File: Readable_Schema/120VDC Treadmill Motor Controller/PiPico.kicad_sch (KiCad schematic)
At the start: 6 parts, among them J3 TB0011-350-08BE, J4 TB0011-350-08BE, J5 TB0011-350-08BE

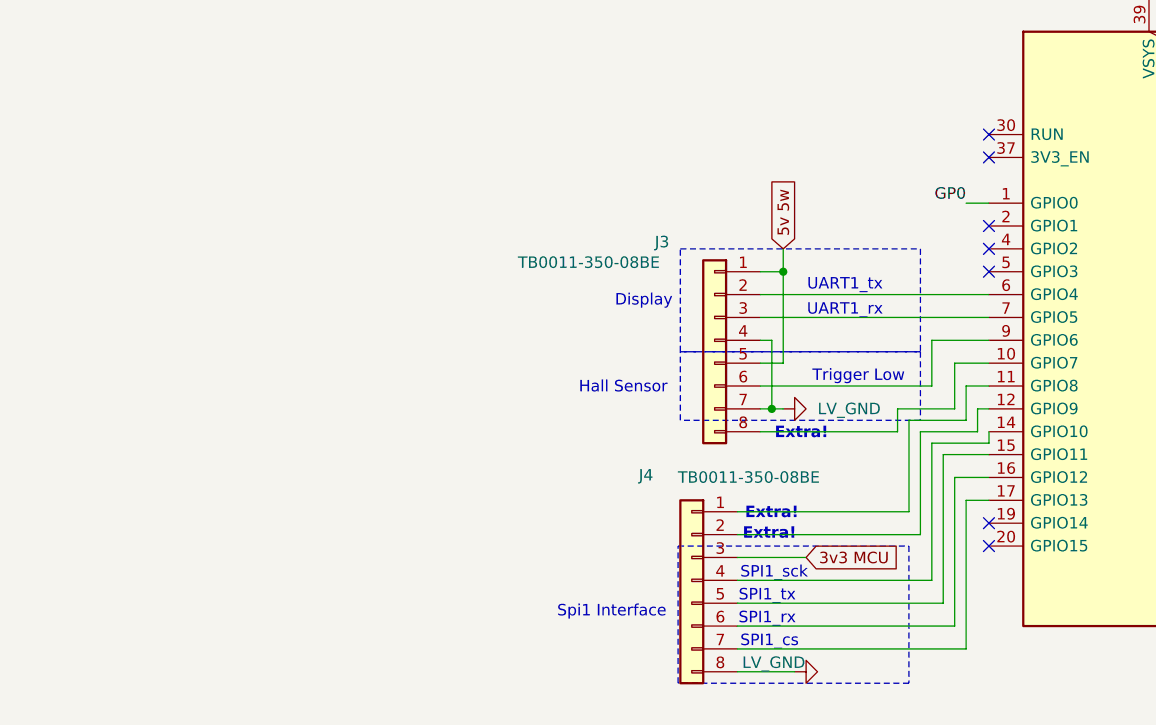
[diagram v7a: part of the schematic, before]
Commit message: -Feedback Schema --fixed some of fine details surrounding pulling some stuff to ground --missing bypass caps --resizing footprints
-H bridge
--Chose higher current rating schottky diode
--Resized footprints and chose better
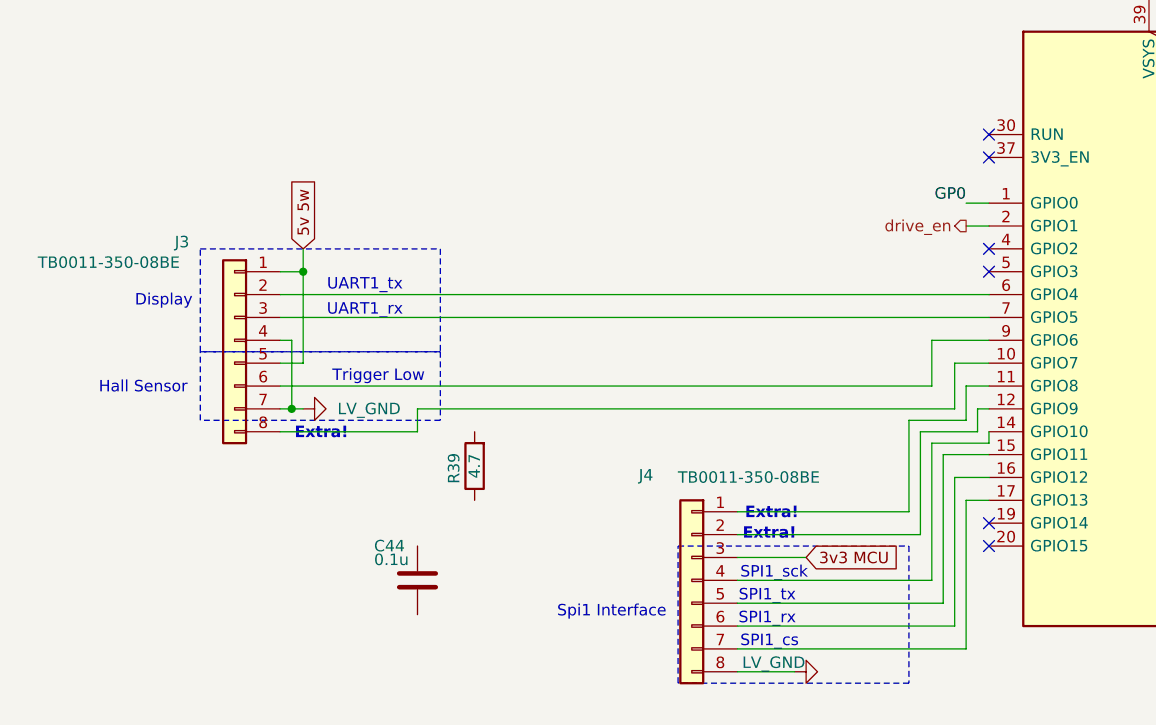
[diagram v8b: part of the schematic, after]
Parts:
- added C44: 0.1u, Capacitor_SMD:C_0201_0603Metric_Pad0.64x0.40mm_HandSolder, symbol Device:C
- added R39: 4.7, Resistor_SMD:R_0201_0603Metric_Pad0.64x0.40mm_HandSolder, symbol Device:R
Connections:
- net drive_en: now reaches A1.2 (GPIO1)
- no-connect marks 9 -> 8
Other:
- moved on the sheet: J3
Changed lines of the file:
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@@
 	(paper "A4")
 	(rectangle
-		(start 83.82 90.17)
-		(end 110.49 101.6)
+		(start 30.48 90.17)
+		(end 57.15 101.6)
 		(stroke
 			(width 0)
@@
 	)
 	(rectangle
-		(start 83.82 101.6)
-		(end 110.49 109.22)
+		(start 30.48 101.6)
+		(end 57.15 109.22)
 		(stroke
 			(width 0)
@@
 	(text "Hall Sensor"
 		(exclude_from_sim no)
-		(at 77.47 105.664 0)
+		(at 24.13 105.664 0)
 		(effects
 			(font
@@
 	(text "UART1_tx"
 		(exclude_from_sim no)
-		(at 102.108 94.234 0)
+		(at 48.768 94.234 0)
 		(effects
 			(font
@@
 	(text "UART1_rx"
 		(exclude_from_sim no)
-		(at 102.108 97.028 0)
+		(at 48.768 97.028 0)
 		(effects
 			(font
@@
 	(text "Display"
 		(exclude_from_sim no)
-		(at 79.756 96.012 0)
+		(at 26.416 96.012 0)
 		(effects
 			(font
@@
 	(text "Trigger Low"
 		(exclude_from_sim no)
-		(at 103.632 104.394 0)
+		(at 50.292 104.394 0)
 		(effects
 			(font
@@
 	(text "Extra!"
 		(exclude_from_sim no)
-		(at 97.282 110.744 0)
+		(at 43.942 110.744 0)
 		(effects
 			(font
@@
 	)
 	(junction
-		(at 95.25 92.71)
+		(at 41.91 92.71)
 		(diameter 0)
 		(color 0 0 0 0)
@@
 	)
 	(junction
-		(at 93.98 107.95)
+		(at 40.64 107.95)
 		(diameter 0)
 		(color 0 0 0 0)
@@
 	)
 	(no_connect
-		(at 118.11 87.63)
-	)
-	(no_connect
 		(at 118.11 90.17)
 	)
@@
 	(wire
 		(pts
-			(xy 92.71 100.33) (xy 93.98 100.33)
+			(xy 39.37 100.33) (xy 40.64 100.33)
 		)
 		(stroke
@@
 	(wire
 		(pts
-			(xy 92.71 97.79) (xy 118.11 97.79)
+			(xy 39.37 97.79) (xy 118.11 97.79)
 		)
 		(stroke
@@
 	(wire
 		(pts
-			(xy 95.25 92.71) (xy 95.25 102.87)
-		)
-		(stroke
-			(width 0)
-			(type default)
-		)
-	)
-	(wire
-		(pts
-			(xy 93.98 100.33) (xy 93.98 107.95)
+			(xy 41.91 92.71) (xy 41.91 102.87)
+		)
+		(stroke
+			(width 0)
+			(type default)
+		)
+	)
+	(wire
+		(pts
+			(xy 40.64 100.33) (xy 40.64 107.95)
 		)
 		(stroke
@@
 	(wire
 		(pts
-			(xy 92.71 110.49) (xy 107.95 110.49)
+			(xy 39.37 110.49) (xy 54.61 110.49)
+		)
+		(stroke
+			(width 0)
+			(type default)
+		)
+	)
+	(wire
+		(pts
+			(xy 115.57 87.63) (xy 118.11 87.63)
 		)
 		(stroke
@@
 	(wire
 		(pts
-			(xy 95.25 107.95) (xy 93.98 107.95)
+			(xy 41.91 107.95) (xy 40.64 107.95)
 		)
 		(stroke
@@
 	(wire
 		(pts
-			(xy 95.25 90.17) (xy 95.25 92.71)
+			(xy 41.91 90.17) (xy 41.91 92.71)
 		)
 		(stroke
@@
 	(wire
 		(pts
-			(xy 107.95 110.49) (xy 107.95 107.95)
+			(xy 54.61 110.49) (xy 54.61 107.95)
 		)
 		(stroke
@@
 	(wire
 		(pts
-			(xy 92.71 107.95) (xy 93.98 107.95)
+			(xy 39.37 107.95) (xy 40.64 107.95)
 		)
 		(stroke
@@
 	(wire
 		(pts
-			(xy 92.71 102.87) (xy 95.25 102.87)
-		)
-		(stroke
-			(width 0)
-			(type default)
-		)
-	)
-	(wire
-		(pts
-			(xy 111.76 105.41) (xy 92.71 105.41)
+			(xy 39.37 102.87) (xy 41.91 102.87)
+		)
+		(stroke
+			(width 0)
+			(type default)
+		)
+	)
+	(wire
+		(pts
+			(xy 111.76 105.41) (xy 39.37 105.41)
 		)
 		(stroke
@@
 	(wire
 		(pts
-			(xy 92.71 92.71) (xy 95.25 92.71)
+			(xy 39.37 92.71) (xy 41.91 92.71)
 		)
 		(stroke
@@
 	(wire
 		(pts
-			(xy 107.95 107.95) (xy 114.3 107.95)
+			(xy 54.61 107.95) (xy 114.3 107.95)
 		)
 		(stroke
@@
 	(wire
 		(pts
-			(xy 92.71 95.25) (xy 118.11 95.25)
+			(xy 39.37 95.25) (xy 118.11 95.25)
 		)
 		(stroke
@@
 	(global_label "5v 5w"
 		(shape input)
-		(at 95.25 90.17 90)
+		(at 41.91 90.17 90)
 		(fields_autoplaced yes)
 		(effects
@@
 		)
 		(property "Intersheetrefs" "${INTERSHEET_REFS}"
-			(at 95.25 81.5001 90)
+			(at 41.91 81.5001 90)
 			(effects
 				(font
@@
 			)
 			(justify left)
+		)
+	)
+	(hierarchical_label "drive_en"
+		(shape output)
+		(at 115.57 87.63 180)
+		(effects
+			(font
+				(size 1.27 1.27)
+			)
+			(justify right)
 		)
 	)
@@
 	(symbol
 		(lib_id "power:GND")
-		(at 95.25 107.95 90)
+		(at 41.91 107.95 90)
 		(unit 1)
 		(exclude_from_sim no)
@@
 		(fields_autoplaced yes)
 		(property "Reference" "#PWR024"
-			(at 101.6 107.95 0)
+			(at 48.26 107.95 0)
 			(effects
 				(font
@@
 		)
 		(property "Value" "LV_GND"
-			(at 99.06 107.9499 90)
+			(at 45.72 107.9499 90)
 			(effects
 				(font
@@
 		)
 		(property "Footprint" ""
-			(at 95.25 107.95 0)
+			(at 41.91 107.95 0)
 			(effects
 				(font
@@
 		)
 		(property "Datasheet" ""
-			(at 95.25 107.95 0)
+			(at 41.91 107.95 0)
 			(effects
 				(font
@@
 		)
 		(property "Description" "Power symbol creates a global label with name \"GND\" , ground"
-			(at 95.25 107.95 0)
+			(at 41.91 107.95 0)
 			(effects
 				(font
@@
 	)
 	(symbol
+		(lib_id "Device:C")
+		(at 54.61 127 0)
+		(unit 1)
+		(exclude_from_sim no)
+		(in_bom yes)
+		(on_board yes)
+		(dnp no)
+		(property "Reference" "C44"
+			(at 49.784 123.19 0)
+			(effects
+				(font
+					(size 1.27 1.27)
+				)
+				(justify left)
+			)
+		)
+		(property "Value" "0.1u"
+			(at 49.784 124.714 0)
+			(effects
+				(font
+					(size 1.27 1.27)
+				)
+				(justify left)
+			)
+		)
+		(property "Footprint" "Capacitor_SMD:C_0201_0603Metric_Pad0.64x0.40mm_HandSolder"
+			(at 55.5752 130.81 0)
+			(effects
+				(font
+					(size 1.27 1.27)
+				)
+				(hide yes)
+			)
+		)
+		(property "Datasheet" "https://mm.digikey.com/Volume0/opasdata/d220001/medias/docus/729/CL05B104KA5NNNC_Spec.pdf"
+			(at 54.61 127 0)
+			(effects
+				(font
+					(size 1.27 1.27)
+				)
+				(hide yes)
+			)
+		)
+		(property "Description" "CL05B104KA5NNNC"
+			(at 54.61 127 0)
+			(effects
+				(font
+					(size 1.27 1.27)
+				)
+				(hide yes)
+			)
+		)
+		(pin "1"
+		)
+		(pin "2"
+		)
+		(instances
+			(project "120VDC Treadmill Motor Controller"
+				(path "/319bc5c0-2dd5-4df3-a34b-9170833ebccd/dc45a2ff-df18-49a4-81ff-80d10381c9e9"
+					(reference "C44")
+					(unit 1)
+				)
+			)
+		)
+	)
+	(symbol
+		(lib_id "Device:R")
+		(at 60.96 114.3 180)
+		(unit 1)
+		(exclude_from_sim no)
+		(in_bom yes)
+		(on_board yes)
+		(dnp no)
+		(property "Reference" "R39"
+			(at 58.674 114.554 90)
+			(effects
+				(font
+					(size 1.27 1.27)
+				)
+			)
+		)
+		(property "Value" "4.7"
+			(at 60.96 114.3 90)
+			(effects
+				(font
+					(size 1.27 1.27)
+				)
+			)
+		)
+		(property "Footprint" "Resistor_SMD:R_0201_0603Metric_Pad0.64x0.40mm_HandSolder"
+			(at 62.738 114.3 90)
+			(effects
+				(font
+					(size 1.27 1.27)
+				)
+				(hide yes)
+			)
+		)
+		(property "Datasheet" "https://industrial.panasonic.com/cdbs/www-data/pdf/RDP0000/AOA0000C337.pdf"
+			(at 60.96 114.3 0)
+			(effects
+				(font
+					(size 1.27 1.27)
+				)
+				(hide yes)
+			)
+		)
+		(property "Description" "ERJ-UP3J100V"
+			(at 60.96 114.3 0)
+			(effects
+				(font
+					(size 1.27 1.27)
+				)
+				(hide yes)
+			)
+		)
+		(pin "1"
+		)
+		(pin "2"
+		)
+		(instances
+			(project "120VDC Treadmill Motor Controller"
+				(path "/319bc5c0-2dd5-4df3-a34b-9170833ebccd/dc45a2ff-df18-49a4-81ff-80d10381c9e9"
+					(reference "R39")
+					(unit 1)
+				)
+			)
+		)
+	)
+	(symbol
 		(lib_id "power:GND")
 		(at 208.28 95.25 270)
@@
 	(symbol
 		(lib_id "Connector_Generic:Conn_01x08")
-		(at 87.63 100.33 0)
+		(at 34.29 100.33 0)
 		(mirror y)
 		(unit 1)
@@
 		(dnp no)
 		(property "Reference" "J3"
-			(at 81.788 89.408 0)
+			(at 28.448 89.408 0)
 			(effects
 				(font
@@
 		)
 		(property "Value" "TB0011-350-08BE"
-			(at 73.66 91.694 0)
+			(at 20.32 91.694 0)
 			(effects
 				(font
@@
 		)
 		(property "Footprint" "Treadmill_Feet:SAMESKY_TB0011-350-08BE"
-			(at 87.63 100.33 0)
+			(at 34.29 100.33 0)
 			(effects
 				(font
@@
 		)
 		(property "Datasheet" "https://www.sameskydevices.com/product/resource/tb0011-350.pdf"
-			(at 87.63 100.33 0)
+			(at 34.29 100.33 0)
 			(effects
 				(font
@@
 		)
 		(property "Description" "Generic connector, single row, 01x08, script generated (kicad-library-utils/schlib/autogen/connector/)"
-			(at 87.63 100.33 0)
-			(effects
-				(font
+			(at 34.29 100.33 0)
+			(effects
+				(font
